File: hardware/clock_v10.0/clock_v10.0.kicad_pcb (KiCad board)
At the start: 2 copper layers, 119 x 92 mm, 217 parts, among them J1 RJ45, J10 KH-BNC50-3511, J11 KH-BNC50-3511, J13 KH-BNC50-3511, J14 DC-005B-2.5A-2.0, J2 Conn_01x03, J3 KH-BNC50-3511, J4 USB_C_Receptacle, J5 Conn_01x06_Pin, J7 KH-BNC50-3511, J9 KH-BNC50-3511, Q1 2N7002, Q10 2N7002, Q9 2N7002, SW1 SW_Push_4PDT, U1 ADA4807-1, U10 STM32F405RGTx, U11 AMS1117-3.3, U12 BA50DD0WHFP-TR, U13 M24C02-RMN, U14 CH340C, U15 USBLC6-2P6, U16 TLV3603DCKR, U17 SN74LVC1G14DBV, U18 TMP112AIDRLR, U19 SN74LVC1G14DBV, U2 SN74LVC1G14DBV, U20 SN74LVC1G14DBV, U21 SN74LVC1G14DBV, U22 MAX40200AUK, U23 TPS63060, U24 MAX40200AUK, U3 SN74LVC1G14DBV, U4 ADA4807-1, U5 ADA4807-1, U6 TLV3603DCKR, U7 SN74LVC1G14DBV, U8 TLV3603DCKR, U9 L78L05_SOT89, Y1 AOCJY4A-10.000MHZ-SW, Y2 16MHz

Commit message: update diodes on clock board
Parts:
- removed U22, U24: MAX40200AUK, Package_TO_SOT_SMD:SOT-23-5
- added D1: SS34, Diode_SMD:D_SMA, F.Cu at (170.0, 86.1)
- added D2: SS34, Diode_SMD:D_SMA, F.Cu at (177.9, 86.1)
- moved TP9 3.92 mm to (181.2, 91.0)
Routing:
- net Net-(D1-K): track 18.9 -> 26.0 mm
- net GND: track 1611.0 -> 1604.6 mm, vias 92 -> 91
- net VBUS: track 118.5 -> 123.7 mm

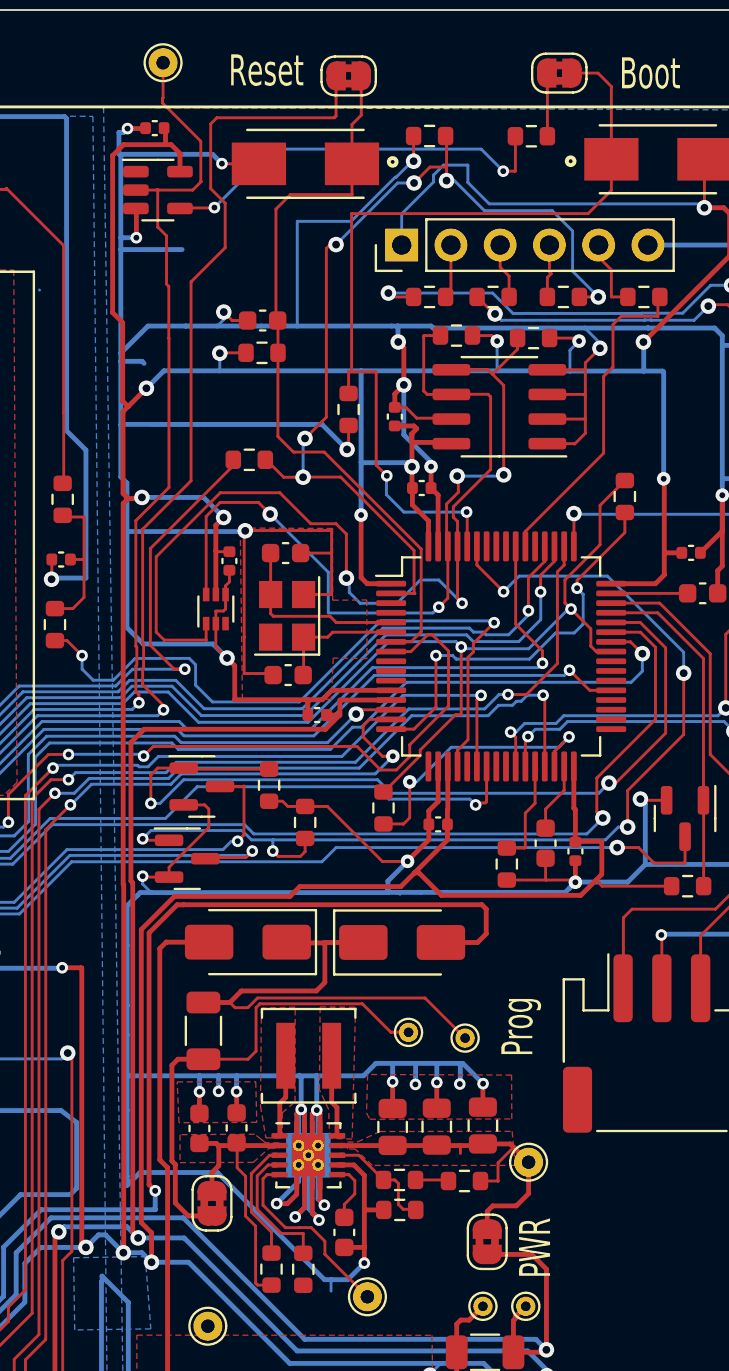
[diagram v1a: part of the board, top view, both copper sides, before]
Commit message: Add PP/LTC Jumper Fixes #275
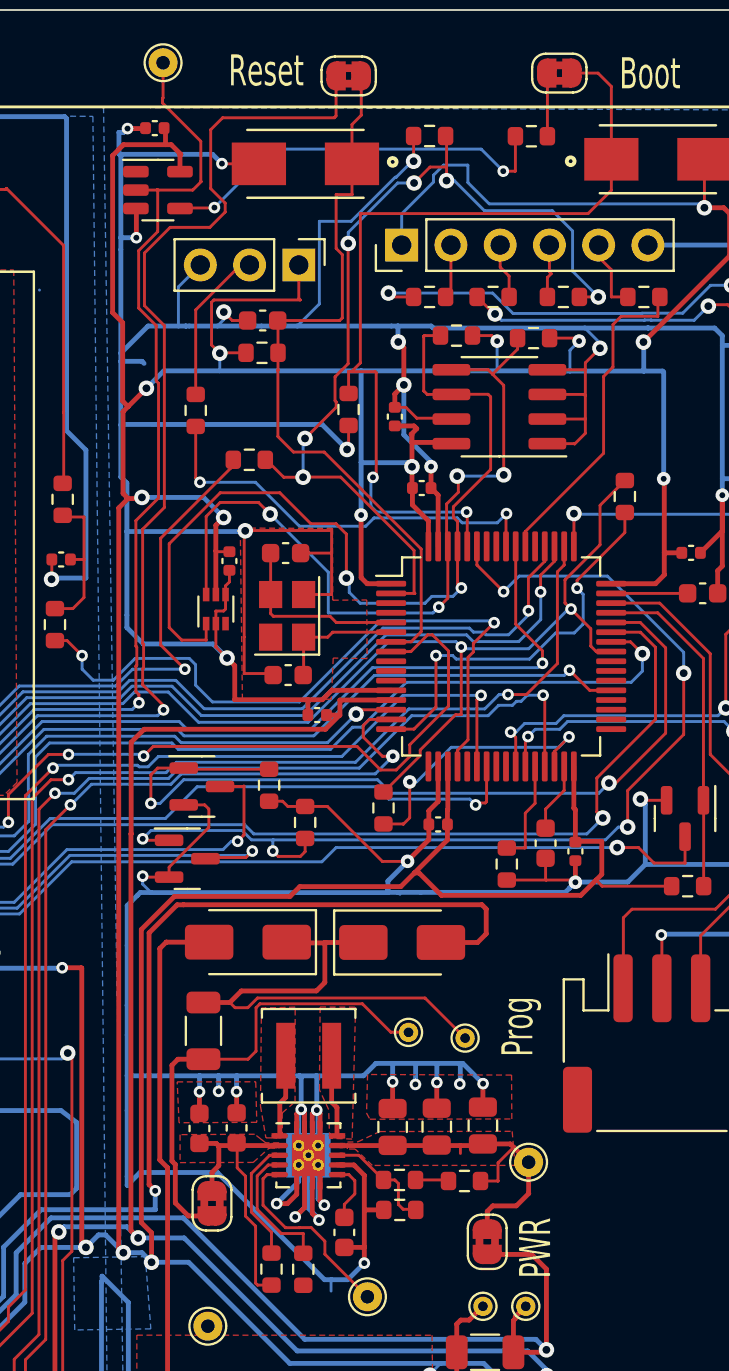
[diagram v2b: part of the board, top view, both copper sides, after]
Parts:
- added J6: Conn_01x03_Pin, Connector_PinHeader_2.54mm:PinHeader_1x03_P2.54mm_Vertical, F.Cu at (172.6, 51.2)
- added R80: 1K0, Resistor_SMD:R_0603_1608Metric, F.Cu at (167.3, 58.7)
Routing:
- net /LED3: track 0.00 -> 21.9 mm, vias 0 -> 2
- net +3.3V: track 505.7 -> 515.1 mm
- net Net-(J6-Pin_2): track 0.00 -> 8.10 mm
- net /SCL: track 48.6 -> 46.0 mm
- net /USB_DTR: track 99.5 -> 101.4 mm
- net /BOOT0: track 45.1 -> 45.9 mm
- net Net-(R72-Pad1): track 78.4 -> 77.7 mm
- net /NRST: track 38.2 -> 38.8 mm

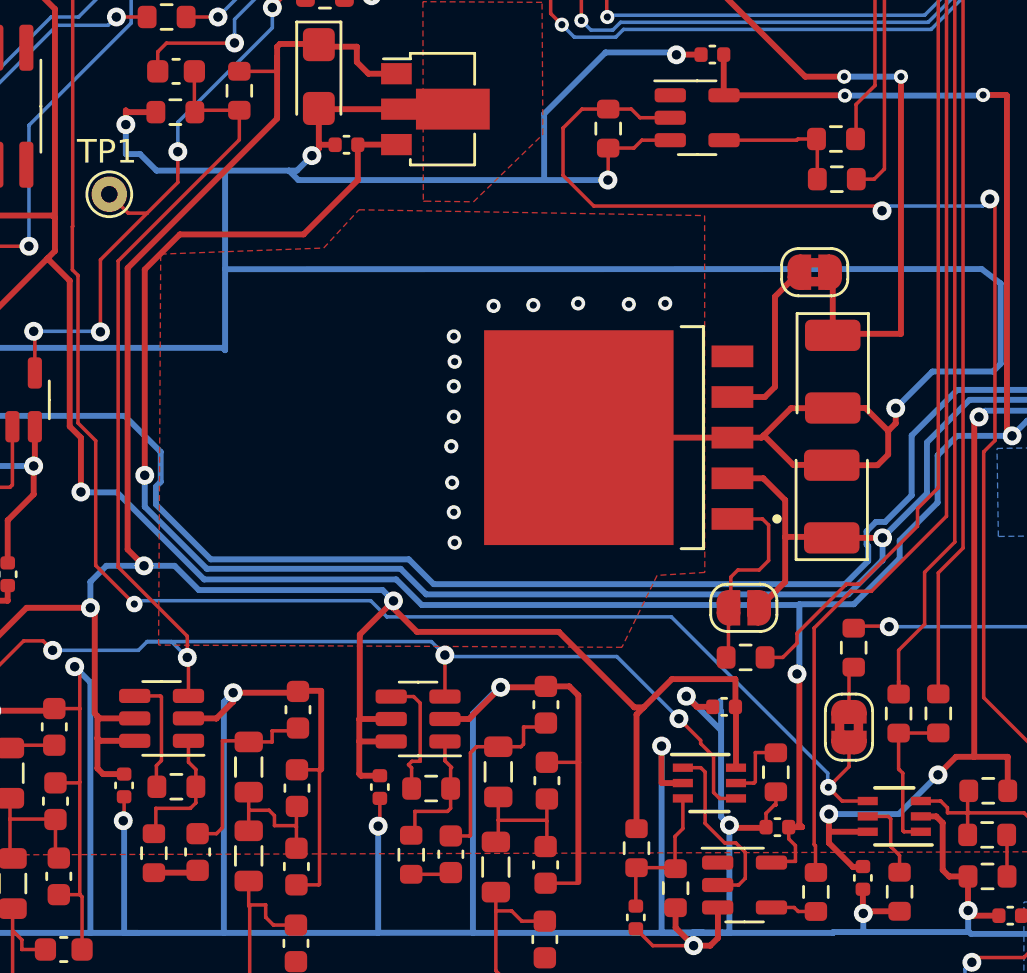
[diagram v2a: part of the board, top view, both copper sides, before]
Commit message: add power sense resisitors Fixes #294
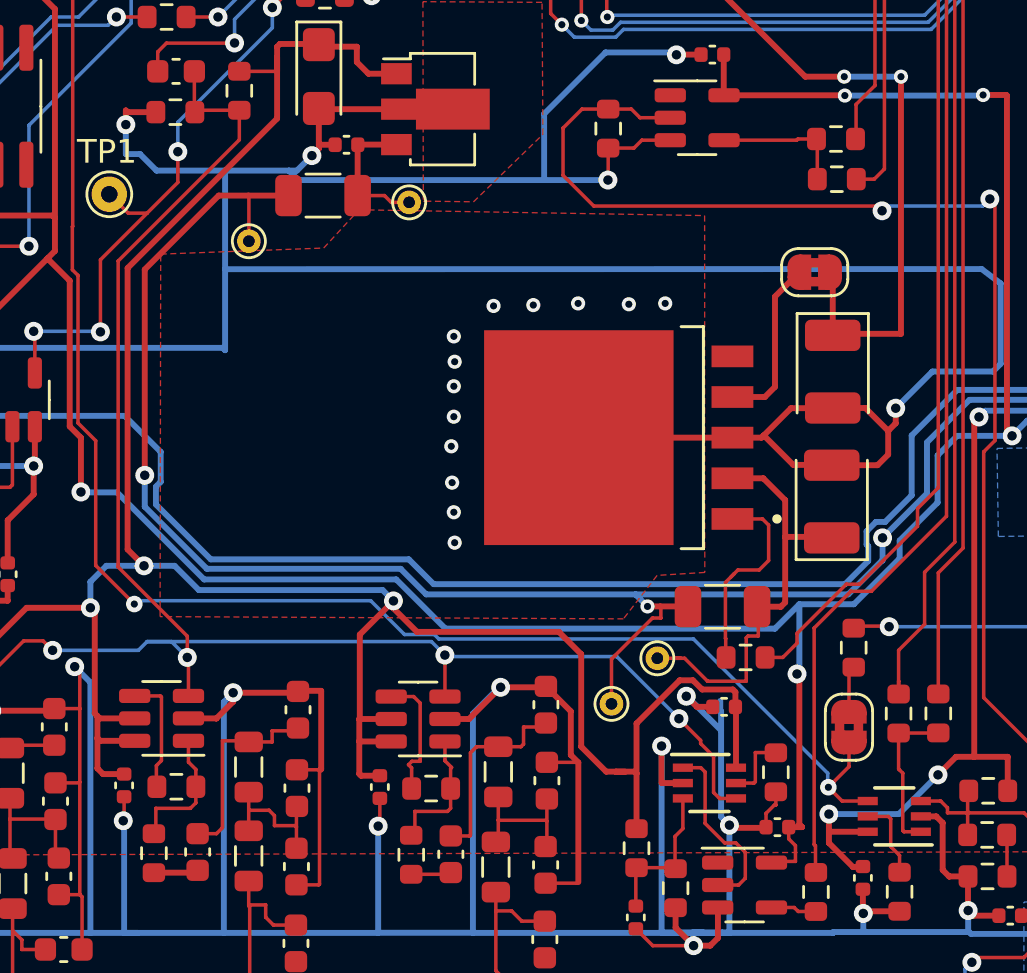
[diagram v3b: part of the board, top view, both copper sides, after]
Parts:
- removed JP5: SolderJumper_2_Open, Jumper:SolderJumper-2_P1.3mm_Open_RoundedPad1.0x1.5mm
- added R81: 0R1, Resistor_SMD:R_1206_3216Metric, F.Cu at (149.3, 109.1)
- added R82: 0R1, Resistor_SMD:R_1206_3216Metric, F.Cu at (132.4, 91.7)
- added TP12: ~, TestPoint:TestPoint_THTPad_D1.0mm_Drill0.5mm, F.Cu at (144.7, 113.2)
- added TP13: ~, TestPoint:TestPoint_THTPad_D1.0mm_Drill0.5mm, F.Cu at (146.6, 111.2)
- added TP14: ~, TestPoint:TestPoint_THTPad_D1.0mm_Drill0.5mm, F.Cu at (129.3, 93.6)
- added TP15: ~, TestPoint:TestPoint_THTPad_D1.0mm_Drill0.5mm, F.Cu at (136.1, 91.9)
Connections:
- C33 pad 2: +6V -> Net-(U9-IN)
- C44 pad 1: +6V -> Net-(U12-VCC)
- U12 pad 2: +6V -> Net-(U12-VCC)
- U9 pad 3: +6V -> Net-(U9-IN)
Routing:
- net Net-(U12-VCC): track 0.00 -> 18.2 mm
- net +6V: track 117.5 -> 109.0 mm, vias 3 -> 4
- net Net-(U9-IN): track 0.00 -> 6.09 mm
- net +5VA: track 130.2 -> 133.2 mm
- net +3.3V: track 515.1 -> 516.0 mm
- net GND: track 1604.4 -> 1603.8 mm

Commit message: add jumper for USB / Reset disconnect Fixes #293
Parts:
- added J8: Conn_01x02_Pin, Connector_PinHeader_2.54mm:PinHeader_1x02_P2.54mm_Vertical, F.Cu at (168.5, 58.5)
- TP2, TP3: footprint TestPoint:TestPoint_THTPad_D1.5mm_Drill0.7mm -> TestPoint:TestPoint_THTPad_D1.0mm_Drill0.5mm
- moved TP3 54.5 mm to (152.7, 141.7)
- moved TP2 36.1 mm to (152.7, 138.7)
- moved R80 2.24 mm to (165.8, 60.3)
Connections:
- TP2 pad 1: /FVIN -> +5VA
- TP3 pad 1: /FVOUT -> +5V
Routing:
- net /USB_DTR: track 101.4 -> 108.4 mm
- net /NRST: track 38.8 -> 41.8 mm
- net Net-(J6-Pin_2): track 8.10 -> 10.4 mm
- net /USB_RTS: track 96.9 -> 97.4 mm

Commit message: moved to 250mW resisotrs. Fixes #289
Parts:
- R15, R16: value 100R -> 100R 250mW; footprint Resistor_SMD:R_0603_1608Metric -> Resistor_SMD:R_1206_3216Metric
- moved TP3 43.1 mm to (157.0, 98.8)
- moved TP2 25.6 mm to (133.7, 121.4)
- moved TP1 7.44 mm to (129.5, 87.3)
- moved R16 7.33 mm to (125.3, 95.4), turned to -90 degrees
- moved R15 4.84 mm to (125.3, 90.5)
- moved C9 1.78 mm to (150.7, 85.7)
- moved R5 1.78 mm to (146.3, 88.8)
- moved U3 1.78 mm to (150.1, 88.4)
- moved C33 0.58 mm to (134.0, 89.4)
- moved C34 0.58 mm to (132.8, 86.5)
- moved U9 0.58 mm to (138.1, 87.9)
- moved TP14 0.53 mm to (128.8, 93.6)
- moved TP15 0.45 mm to (135.6, 92.0)
- moved R82 0.44 mm to (132.0, 91.6)
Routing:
- net +5VA: track 133.2 -> 140.7 mm
- net Net-(R56-Pad2): track 24.9 -> 30.6 mm
- net +3.3V: track 516.0 -> 510.9 mm
- net GND: track 1603.8 -> 1608.5 mm
- net +5V: track 136.1 -> 139.4 mm
- net Net-(R63-Pad2): track 5.65 -> 2.57 mm
- net /10Mhz2.5V: track 74.5 -> 76.8 mm
- net Net-(J9-In): track 113.8 -> 111.7 mm

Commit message: fiux voltage dirvide for GPS TX. Fixes #260
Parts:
- R35: value 2K2 -> 3K3
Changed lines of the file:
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@@
     (descr "Resistor SMD 0603 (1608 Metric), square (rectangular) end terminal, IPC_7351 nominal, (Body size source: IPC-SM-782 page 72, https://www.pcb-3d.com/wordpress/wp-content/uploads/ipc-sm-782a_amendment_1_and_2.pdf), generated with kicad-footprint-generator")
     (tags "resistor")
-    (property "JLCPCB Part #" "C4190")
-    (property "LCSC" "")
+    (property "JLCPCB Part #" "C22978")
     (property "Sheetfile" "clock_v10.0.kicad_sch")
     (property "Sheetname" "")
@@
         (effects (font (size 1 1) (thickness 0.15)))
     )
-    (fp_text value "2K2" (at 0 1.43 90) (layer "F.Fab")
+    (fp_text value "3K3" (at 0 1.43 90) (layer "F.Fab")
         (effects (font (size 1 1) (thickness 0.15)))
     )

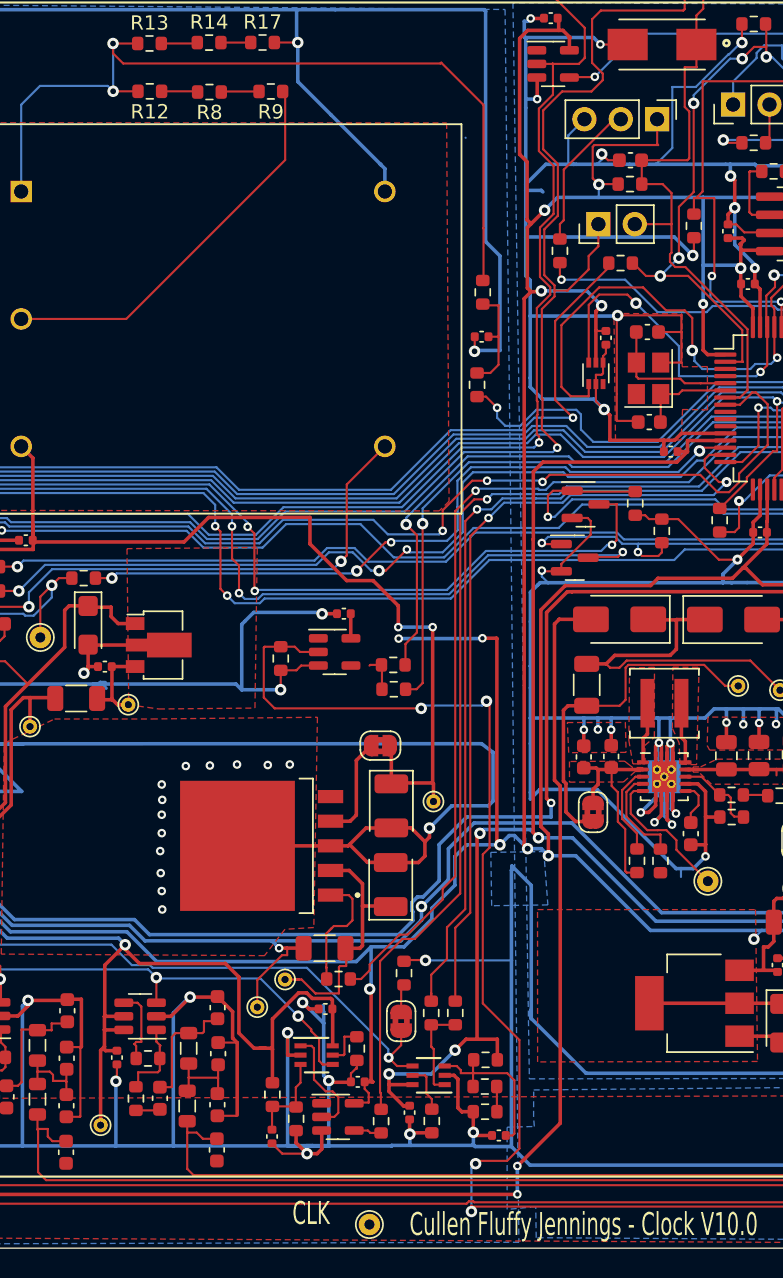
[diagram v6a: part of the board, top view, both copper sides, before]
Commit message: fix up clock board errors
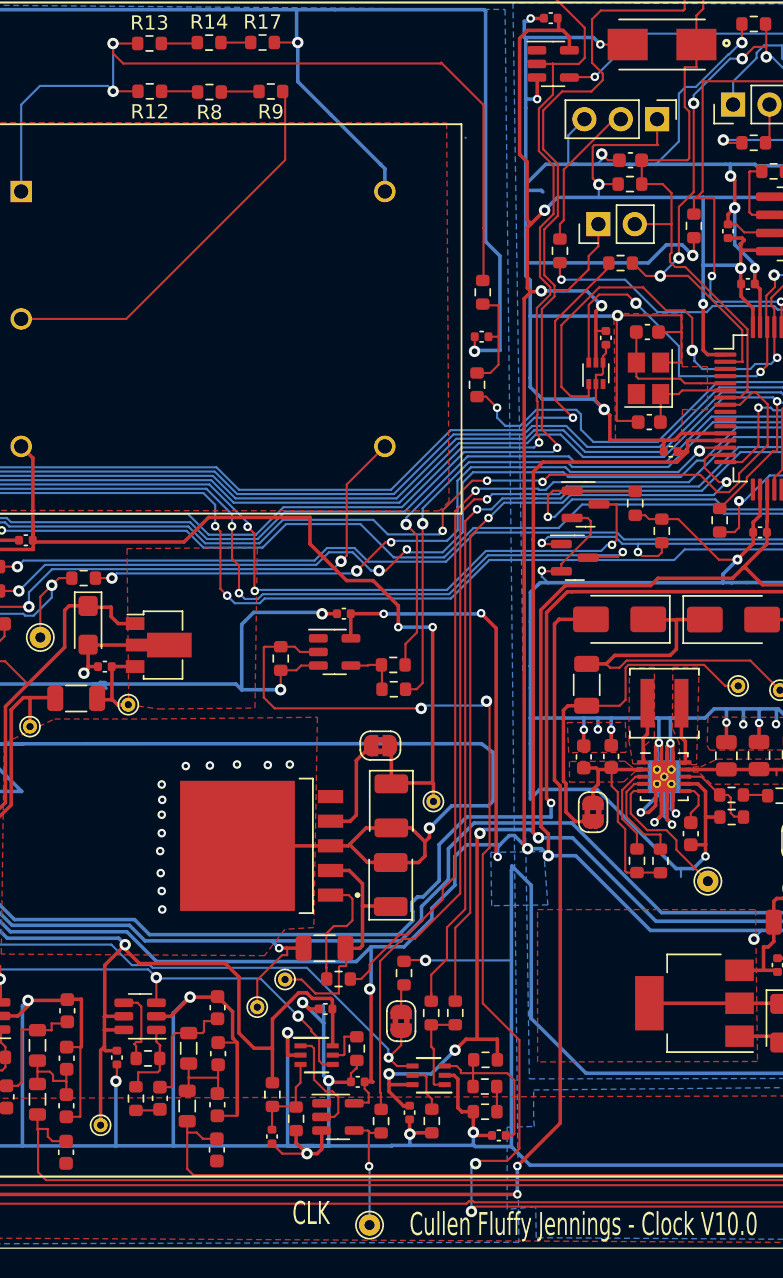
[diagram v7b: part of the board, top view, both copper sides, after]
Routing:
- net GND: track 1608.5 -> 1597.6 mm
- net Net-(R57-Pad2): track 1.95 -> 8.52 mm, vias 0 -> 1
- net +3.3V: track 510.9 -> 517.0 mm
- net /FVIN: track 15.2 -> 16.8 mm
- net Net-(R63-Pad2): track 2.57 -> 3.87 mm
- net +6V: vias 4 -> 3
